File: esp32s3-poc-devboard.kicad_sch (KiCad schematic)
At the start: 99 parts, among them J1 24VDC, J2 Conn_01x01_Pin, J3 USB_C_Receptacle_USB2.0_14P, J4 USB_C_Receptacle_USB2.0_14P, J5 Screw_Terminal_01x06, J6 Conn_Coaxial, J7 Conn_01x16_Pin, J8 Screw_Terminal_01x04, Q3 MMDT5551, SW1 SW_Push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

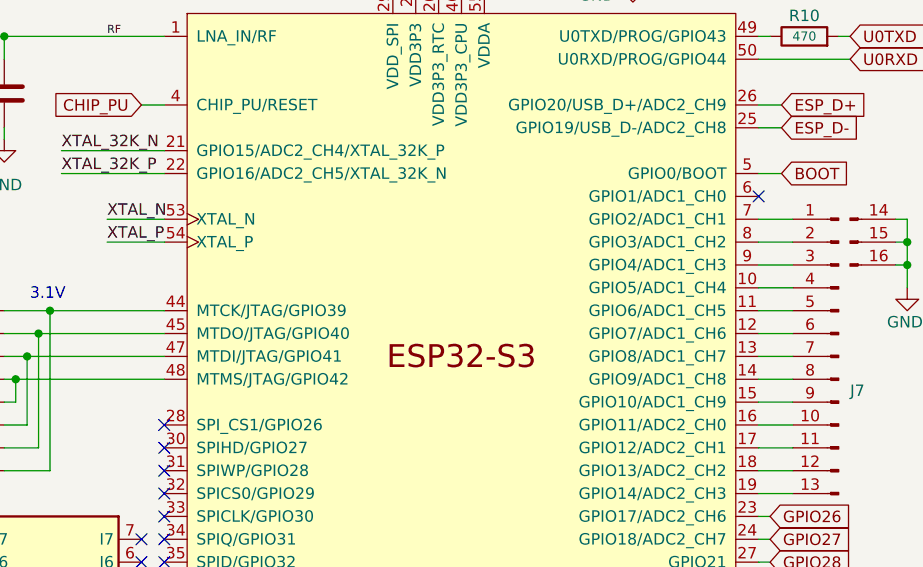
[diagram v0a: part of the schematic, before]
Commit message: schem: move 24v input to ADC pins
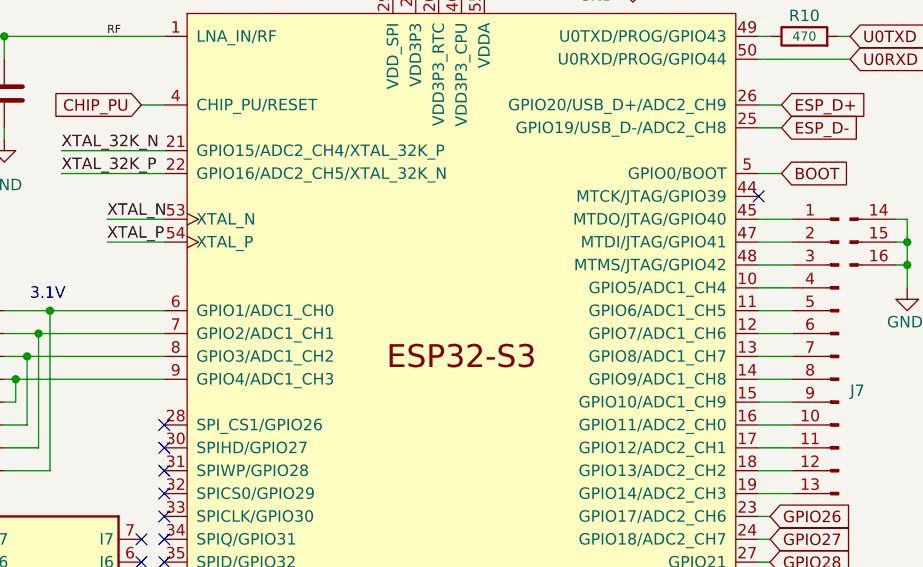
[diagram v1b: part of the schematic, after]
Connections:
- net at R24.2, R31.1: now also U1.6 (GPIO1/ADC1_CH0); no longer U1.44 (MTCK/JTAG/GPIO39)
- net at R25.1, R28.2: now also U1.9 (GPIO4/ADC1_CH3); no longer U1.48 (MTMS/JTAG/GPIO42)
- net at J7.1 (Pin_1): now also U1.45 (MTDO/JTAG/GPIO40); no longer U1.7 (GPIO2/ADC1_CH1)
- net at J7.2 (Pin_2): now also U1.47 (MTDI/JTAG/GPIO41); no longer U1.8 (GPIO3/ADC1_CH2)
- net at J7.3 (Pin_3): now also U1.48 (MTMS/JTAG/GPIO42); no longer U1.9 (GPIO4/ADC1_CH3)
- net at R27.2, R29.1: now also U1.8 (GPIO3/ADC1_CH2); no longer U1.47 (MTDI/JTAG/GPIO41)
- net at R26.2, R30.1: now also U1.7 (GPIO2/ADC1_CH1); no longer U1.45 (MTDO/JTAG/GPIO40)

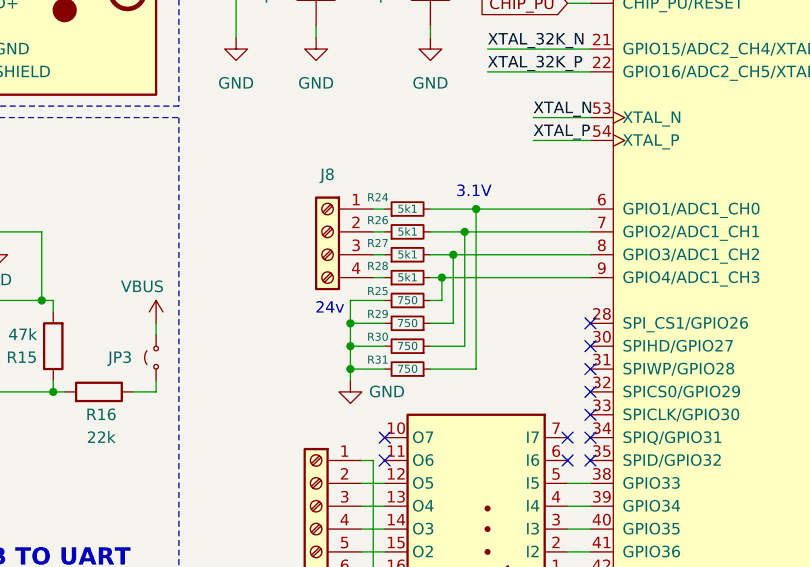
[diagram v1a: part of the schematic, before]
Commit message: schem: add 3v3 protection diodes to adc pins
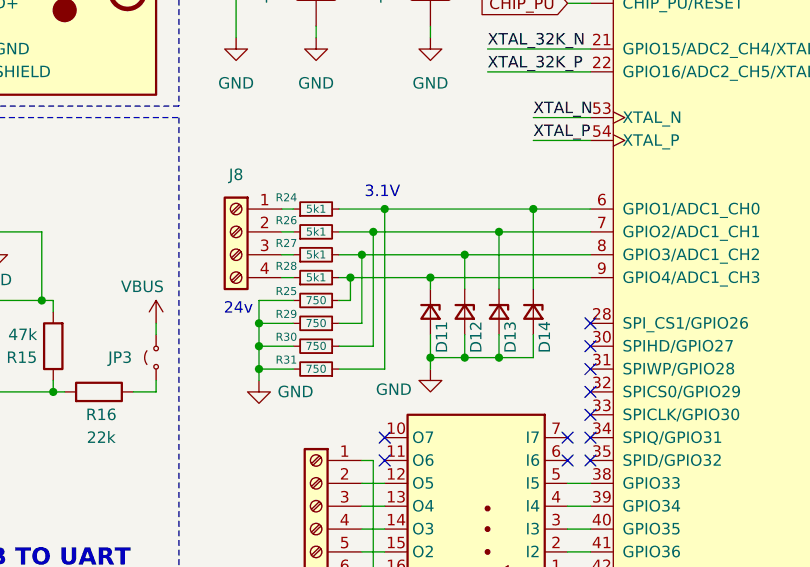
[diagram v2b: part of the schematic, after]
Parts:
- added D11, D12, D13, D14: BZT52B3V3, Diode_SMD:D_SOD-123, symbol Device:D_Zener_Small
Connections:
- net GND: now also D11.2 (A), D12.2 (A), D13.2 (A), D14.2 (A)
- net at R24.2, R31.1, U1.6 (GPIO1/ADC1_CH0): now also D14.1 (K)
- net at R25.1, R28.2, U1.9 (GPIO4/ADC1_CH3): now also D11.1 (K)
- net at R27.2, R29.1, U1.8 (GPIO3/ADC1_CH2): now also D12.1 (K)
- net at R26.2, R30.1, U1.7 (GPIO2/ADC1_CH1): now also D13.1 (K)
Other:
- moved on the sheet: J8, R24, R25, R26, R27, R28, R29, R30, R31

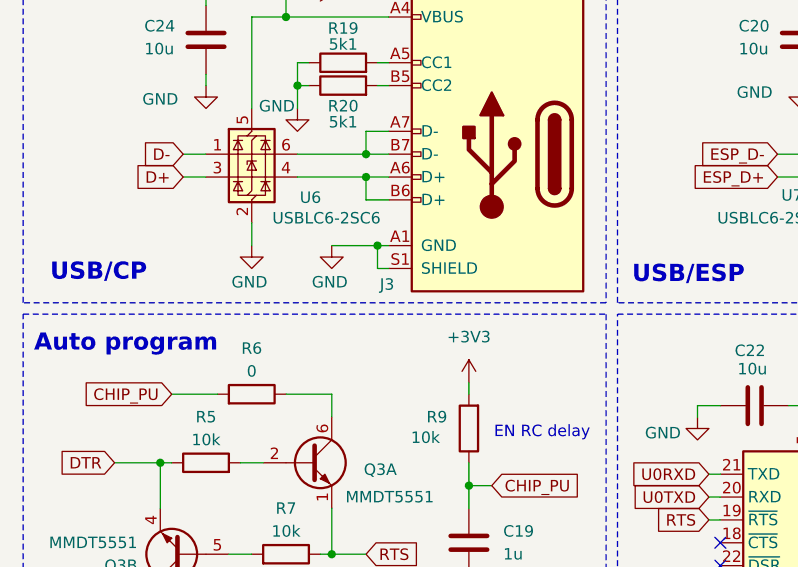
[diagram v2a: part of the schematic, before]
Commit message: schem: update USBC symbol
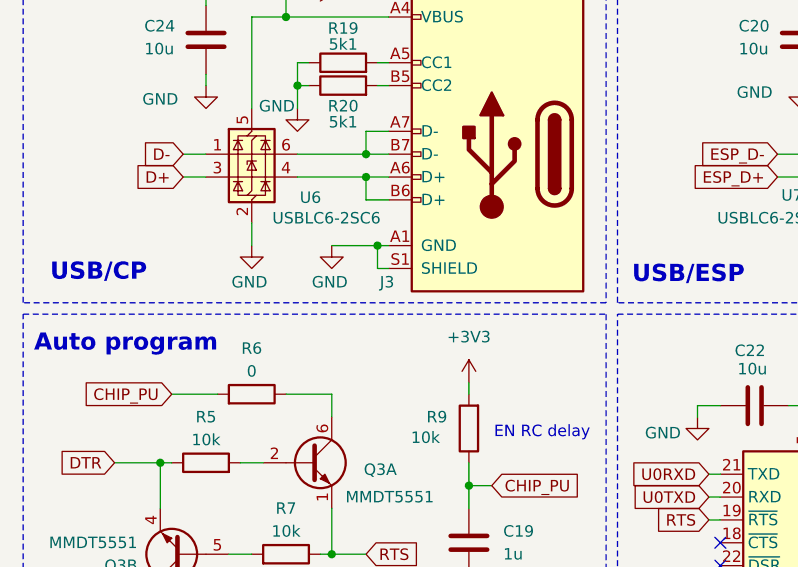
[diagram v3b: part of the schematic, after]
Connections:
- net GND: now also J3.A12 (GND), J3.B1 (GND), J3.B12 (GND), J4.A12 (GND), J4.B1 (GND), J4.B12 (GND)
- net VBUS: now also J3.A9 (VBUS), J3.B4 (VBUS), J3.B9 (VBUS), J4.A9 (VBUS), J4.B4 (VBUS), J4.B9 (VBUS)

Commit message: schem: update spare gpio pins
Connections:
- net GND: now also J7.1 (Pin_1), J7.2 (Pin_2), J7.3 (Pin_3)
- net at U1.45 (MTDO/JTAG/GPIO40): no longer J7.1 (Pin_1)
- net at U1.47 (MTDI/JTAG/GPIO41): no longer J7.2 (Pin_2)
- net at U1.48 (MTMS/JTAG/GPIO42): no longer J7.3 (Pin_3)
- no-connect marks 22 -> 25
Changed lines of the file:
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@@
 	)
 	(junction
+		(at 261.62 83.82)
+		(diameter 0)
+		(color 0 0 0 0)
+	)
+	(junction
 		(at 72.39 147.32)
 		(diameter 0)
@@
 	)
 	(junction
+		(at 261.62 81.28)
+		(diameter 0)
+		(color 0 0 0 0)
+	)
+	(junction
 		(at 120.65 66.04)
 		(diameter 0)
@@
 	)
 	(junction
+		(at 275.59 81.28)
+		(diameter 0)
+		(color 0 0 0 0)
+	)
+	(junction
 		(at 179.07 107.95)
 		(diameter 0)
@@
 	)
 	(no_connect
+		(at 259.08 81.28)
+	)
+	(no_connect
 		(at 193.04 111.76)
 	)
@@
 	)
 	(no_connect
+		(at 259.08 86.36)
+	)
+	(no_connect
 		(at 93.98 114.3)
 	)
@@
 	)
 	(no_connect
+		(at 259.08 83.82)
+	)
+	(no_connect
 		(at 190.5 116.84)
 	)
@@
 	(wire
 		(pts
+			(xy 261.62 81.28) (xy 262.89 81.28)
+		)
+		(stroke
+			(width 0)
+			(type default)
+		)
+	)
+	(wire
+		(pts
 			(xy 55.88 73.66) (xy 57.15 73.66)
 		)
@@
 	(wire
 		(pts
+			(xy 275.59 78.74) (xy 275.59 81.28)
+		)
+		(stroke
+			(width 0)
+			(type default)
+		)
+	)
+	(wire
+		(pts
 			(xy 259.08 109.22) (xy 262.89 109.22)
 		)
@@
 	(wire
 		(pts
+			(xy 261.62 83.82) (xy 262.89 83.82)
+		)
+		(stroke
+			(width 0)
+			(type default)
+		)
+	)
+	(wire
+		(pts
 			(xy 160.02 106.68) (xy 156.21 106.68)
 		)
@@
 	(wire
 		(pts
-			(xy 259.08 86.36) (xy 262.89 86.36)
-		)
-		(stroke
-			(width 0)
-			(type default)
-		)
-	)
-	(wire
-		(pts
 			(xy 90.17 181.61) (xy 95.25 181.61)
 		)
@@
 	(wire
 		(pts
-			(xy 259.08 81.28) (xy 262.89 81.28)
-		)
-		(stroke
-			(width 0)
-			(type default)
-		)
-	)
-	(wire
-		(pts
 			(xy 180.34 35.56) (xy 180.34 34.29)
 		)
@@
 	(wire
 		(pts
-			(xy 259.08 83.82) (xy 262.89 83.82)
-		)
-		(stroke
-			(width 0)
-			(type default)
-		)
-	)
-	(wire
-		(pts
 			(xy 226.06 38.1) (xy 227.33 38.1)
 		)
@@
 	(wire
 		(pts
+			(xy 261.62 81.28) (xy 261.62 78.74)
+		)
+		(stroke
+			(width 0)
+			(type default)
+		)
+	)
+	(wire
+		(pts
 			(xy 100.33 179.07) (xy 100.33 181.61)
 		)
@@
 	(wire
 		(pts
+			(xy 261.62 78.74) (xy 275.59 78.74)
+		)
+		(stroke
+			(width 0)
+			(type default)
+		)
+	)
+	(wire
+		(pts
 			(xy 64.77 25.4) (xy 64.77 24.13)
 		)
@@
 	(wire
 		(pts
+			(xy 262.89 86.36) (xy 261.62 86.36)
+		)
+		(stroke
+			(width 0)
+			(type default)
+		)
+	)
+	(wire
+		(pts
 			(xy 120.65 66.04) (xy 123.19 66.04)
 		)
@@
 	(wire
 		(pts
+			(xy 261.62 83.82) (xy 261.62 81.28)
+		)
+		(stroke
+			(width 0)
+			(type default)
+		)
+	)
+	(wire
+		(pts
 			(xy 107.95 24.13) (xy 105.41 24.13)
 		)
@@
 		)
 		(stroke
+			(width 0)
+			(type default)
+		)
+	)
+	(wire
+		(pts
+			(xy 261.62 86.36) (xy 261.62 83.82)
+		)
+		(stroke

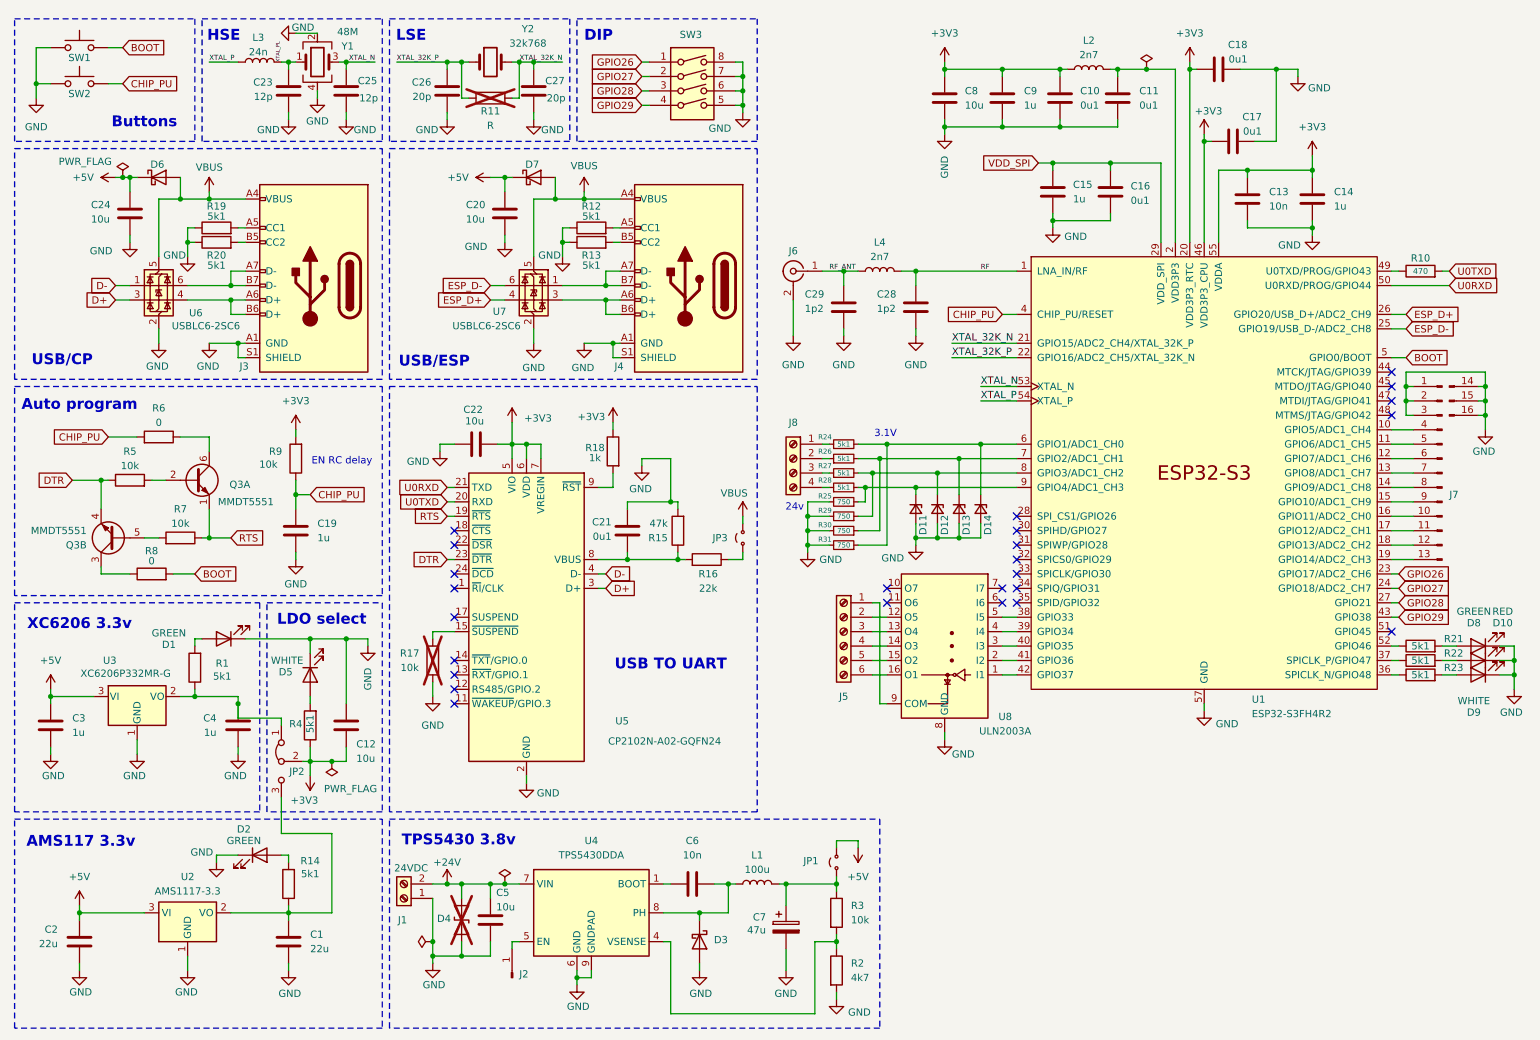
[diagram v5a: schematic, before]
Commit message: schem: add fiducials, mounting and tooling holes
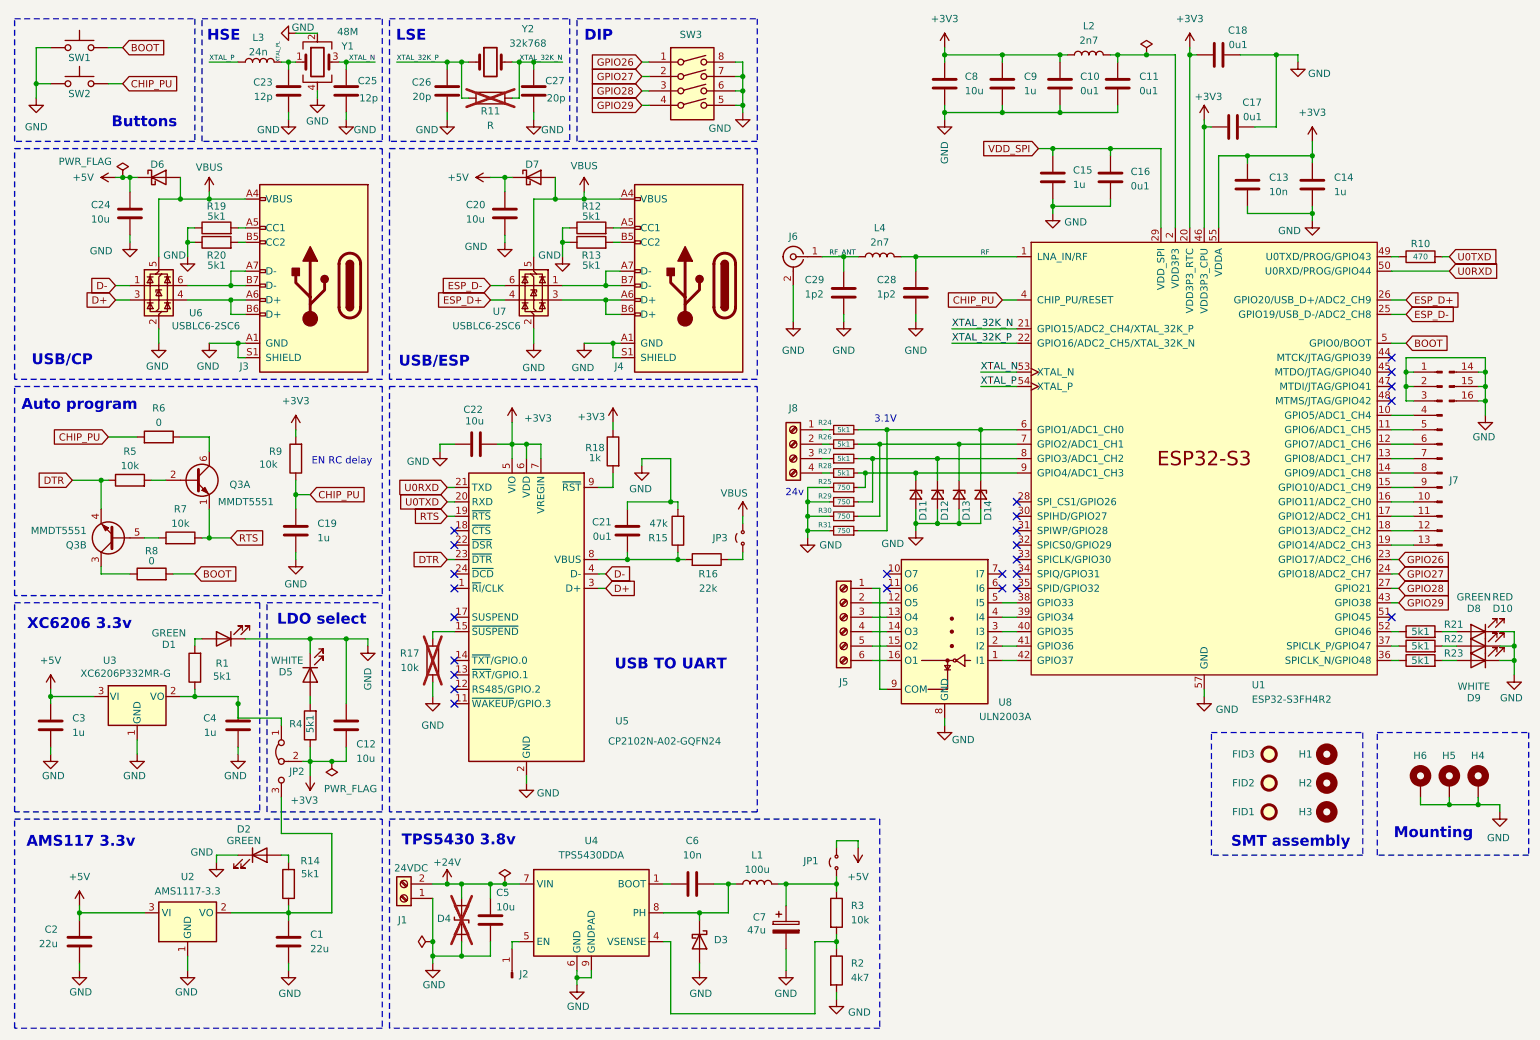
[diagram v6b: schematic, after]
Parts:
- added FID1, FID2, FID3: Fiducial, Fiducial:Fiducial_1mm_Mask2mm, symbol Mechanical:Fiducial
- added H1, H2, H3: MountingHole, MountingHole:ToolingHole_1.152mm, symbol Mechanical:MountingHole
- added H4, H5, H6: MountingHole_Pad, MountingHole:MountingHole_2.2mm_M2_Pad_Via, symbol Mechanical:MountingHole_Pad
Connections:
- net GND: now also H4.1, H5.1, H6.1
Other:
- note added: "Mounting"
- note added: "SMT assembly"
- moved on the sheet: C10, C11, C13, C14, C15, C16, C17, C18, C28, C29, C8, C9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
